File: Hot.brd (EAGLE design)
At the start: 69.5 x 57.1 mm, 21 parts, among them Q1 BC817, T1 BTA24-600

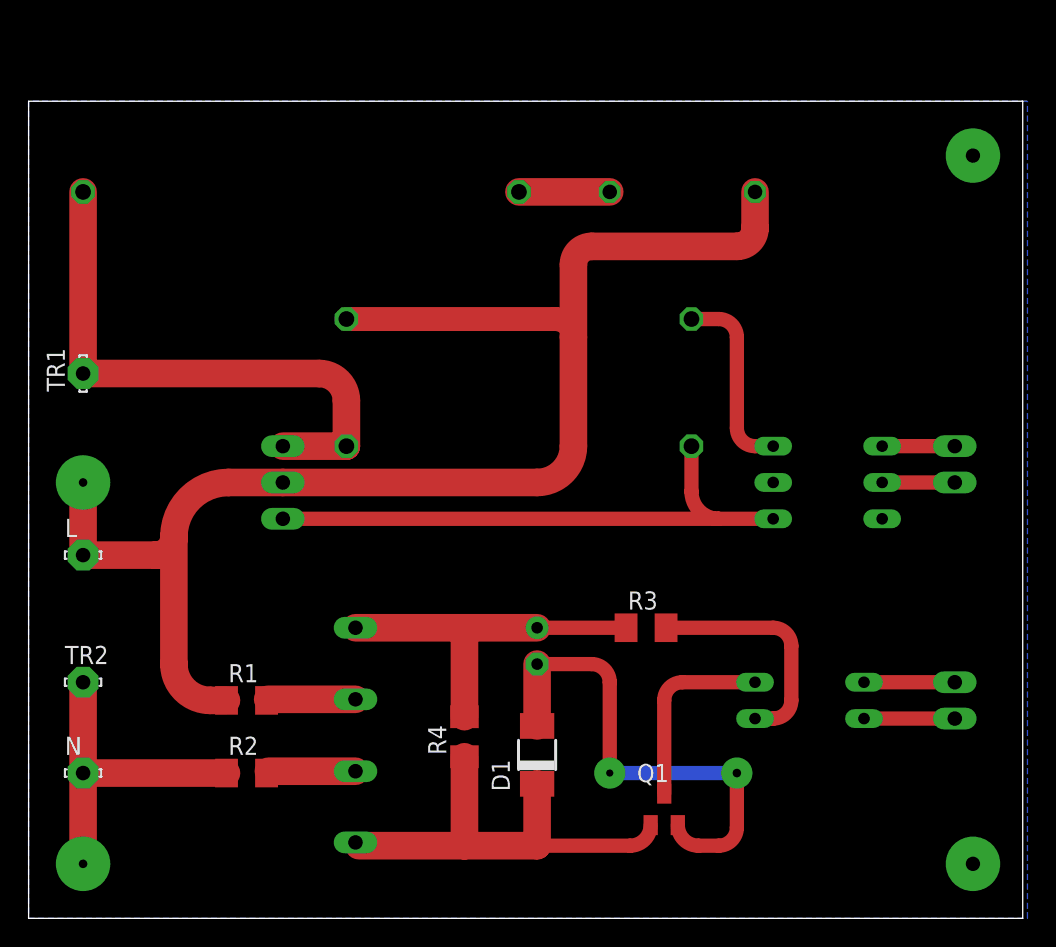
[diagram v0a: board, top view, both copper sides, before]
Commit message: Переразвел 2горячую" плату - уменьшил длинну упарвляющей дорожки, увеличил ширину силовых дорожек. Под тиристором уменьшились зазоры - на перетрав, при необходимости - доработать напильником %) Добавил подписи "+" на разъемах
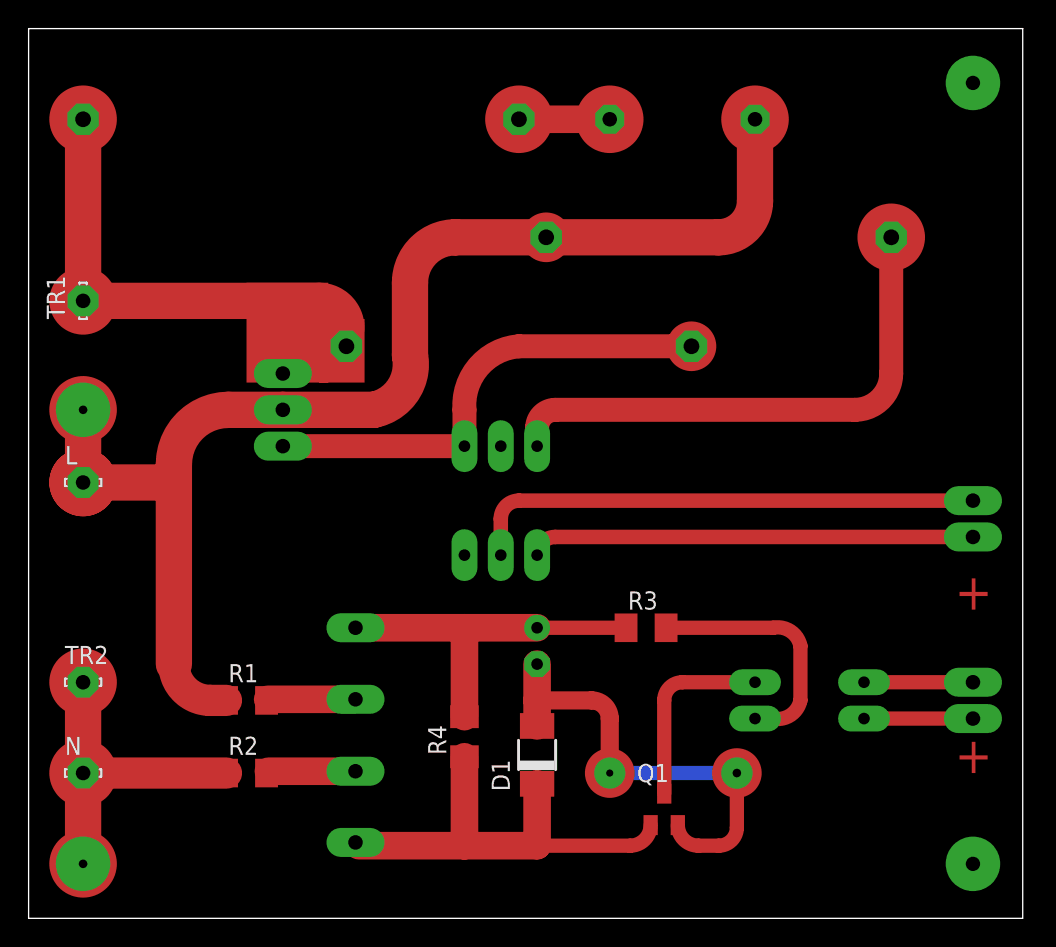
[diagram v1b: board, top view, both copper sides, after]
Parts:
- C1: value 10u/10V -> 10u/16V
- moved MOC3061 22.9 mm to (33.0, 29.2), turned to 0 degrees
- moved R6 15.1 mm to (48.3, 47.6)
- moved R7 6.98 mm to (34.3, 40.0)
- moved CX1 5.08 mm to (45.7, 55.9)
- moved R8 5.08 mm to (19.1, 55.9)
- moved L 5.08 mm to (3.81, 30.5)
- moved T1 5.08 mm to (15.2, 35.6)
- moved TR1 5.08 mm to (3.81, 43.2)
- moved TO_MOC3061_2 4.02 mm to (66.0, 27.9), turned to 90 degrees
- moved TO_4N33_2 1.27 mm to (66.0, 15.2)
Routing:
- net N$29: track 5.08 -> 36.1 mm
- net TO_MOC3061: track 5.08 -> 31.0 mm
- net N$9: track 13.1 -> 37.1 mm
- net L: track 101.5 -> 88.1 mm
- net N$8: track 40.2 -> 33.2 mm
- net N$2: track 34.2 -> 31.7 mm
- net N$11: track 39.5 -> 38.0 mm
- net N$27: track 6.35 -> 7.62 mm
- net N$12: track 6.35 -> 7.62 mm
- net N$3: track 16.2 -> 17.1 mm
- removed copper zone on layer 16, net GND
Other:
- board size 69.5 x 57.1 mm -> 69.5 x 62.2 mm
- board text added: "+"
